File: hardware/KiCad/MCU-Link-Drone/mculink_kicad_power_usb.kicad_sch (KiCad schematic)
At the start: 39 parts, among them J9 USB4110-GF-A_REVB, U1 LPC55S69JBD64, U2 XC6227C331PR-G, Y1 16.000MHz

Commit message: updated with drone project files
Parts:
- J9: footprint mculink:GCT_USB4110-GF-A_REVB -> Connector_USB:USB_C_Receptacle_GCT_USB4110
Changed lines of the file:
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@@
 			)
 		)
-		(property "Footprint" "mculink:GCT_USB4110-GF-A_REVB"
+		(property "Footprint" "Connector_USB:USB_C_Receptacle_GCT_USB4110"
 			(at -62.23 198.12 0)
 			(effects

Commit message: worked on layout
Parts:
- J9: footprint Connector_USB:USB_C_Receptacle_GCT_USB4110 -> McuOnEclipse:USB_C_Receptacle_GCT_USB4110-GF-A
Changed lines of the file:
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@@
 			)
 		)
-		(property "Footprint" "Connector_USB:USB_C_Receptacle_GCT_USB4110"
+		(property "Footprint" "McuOnEclipse:USB_C_Receptacle_GCT_USB4110-GF-A"
 			(at -62.23 198.12 0)
 			(effects

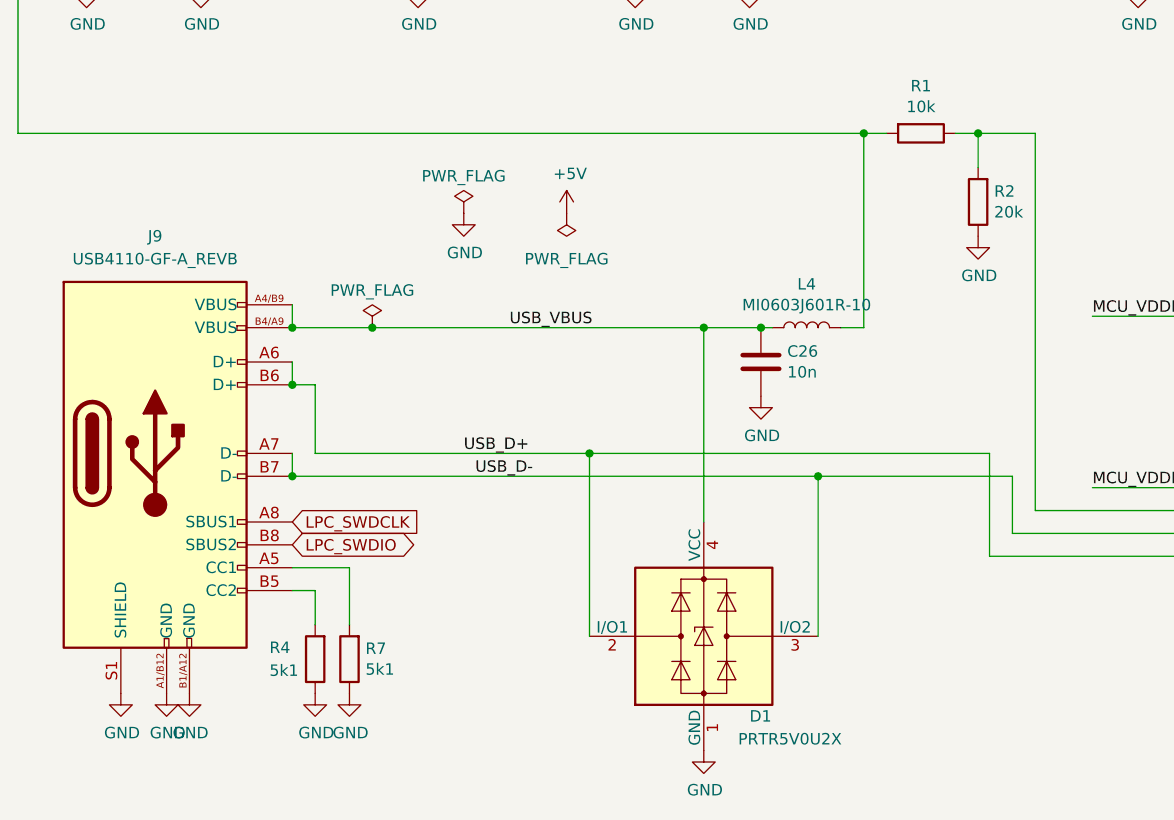
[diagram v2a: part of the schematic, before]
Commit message: fixed warnings
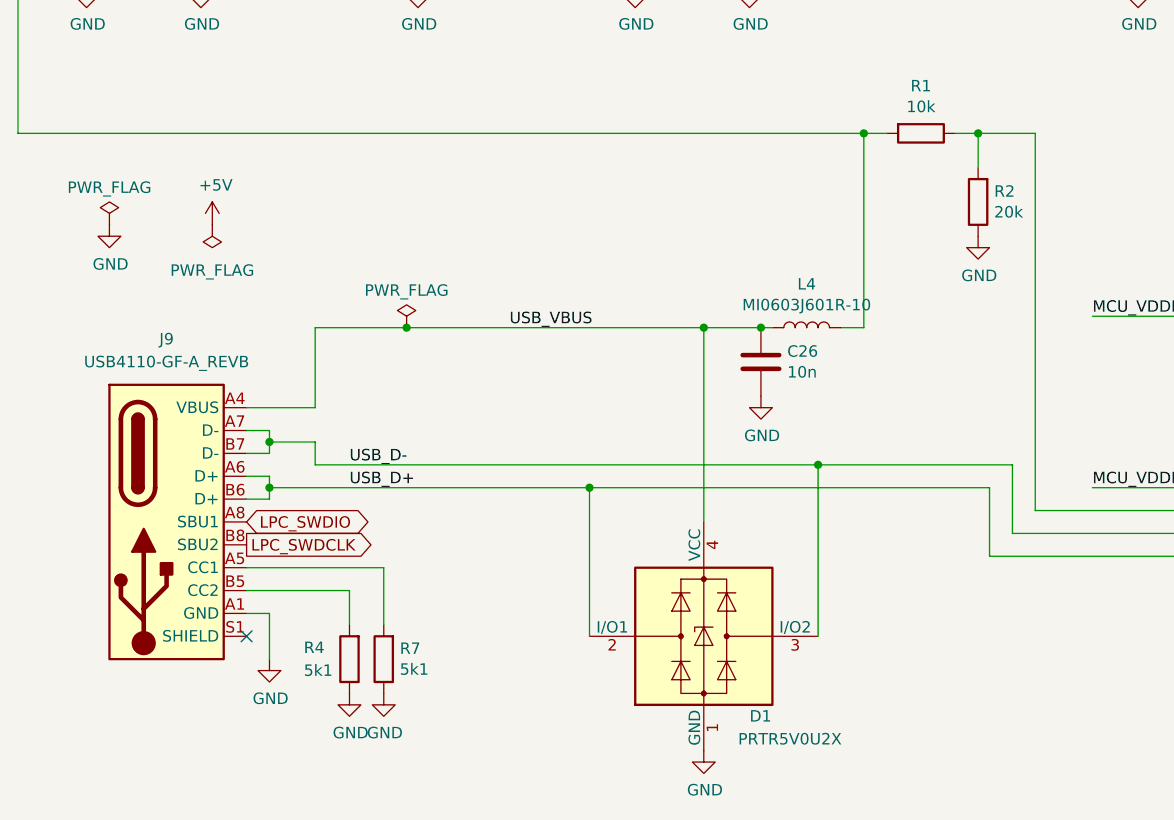
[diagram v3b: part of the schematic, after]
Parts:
- J9: symbol McuOnEclipse:USB4110-GF-A_REVB -> McuOnEclipse:USB_C_Receptacle_GCT_USB4110-GF-A; MFR (none) -> GCT; MFR# (none) -> USB4110-GF-A; mouser# (none) -> 640-USB4110-GF-A
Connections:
- net GND: now also J9.A1 (GND), J9.A12 (GND), J9.B1 (GND), J9.B12 (GND); no longer J9.A1/B12 (GND), J9.B1/A12 (GND), J9.S1 (SHIELD)
- net LPC_SWDCLK: now also J9.B8 (SBU2); no longer J9.A8 (SBUS1)
- net LPC_SWDIO: now also J9.A8 (SBU1); no longer J9.B8 (SBUS2)
- net USB_VBUS: now also J9.A4 (VBUS), J9.A9 (VBUS), J9.B4 (VBUS), J9.B9 (VBUS); no longer J9.A4/B9 (VBUS), J9.B4/A9 (VBUS)
- no-connect marks 4 -> 5
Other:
- moved on the sheet: R4, R7

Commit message: added 3D models
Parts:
- U2: footprint Package_TO_SOT_SMD:SOT-89-5 -> McuOnEclipse:SOT-89-5
- Y1: footprint mculink_kicad:CX3225GA16000D0PTVCC -> McuOnEclipse:CX3225GA16000D0PTVCC
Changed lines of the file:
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@@
 			)
 		)
-		(property "Footprint" "mculink_kicad:CX3225GA16000D0PTVCC"
+		(property "Footprint" "McuOnEclipse:CX3225GA16000D0PTVCC"
 			(at 241.3 48.26 0)
 			(effects
@@
 			)
 		)
-		(property "Footprint" "Package_TO_SOT_SMD:SOT-89-5"
+		(property "Footprint" "McuOnEclipse:SOT-89-5"
 			(at 54.61 82.55 0)
 			(effects

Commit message: fixed warnings
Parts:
- R4, R7: footprint Resistor_SMD:R_0402_1005Metric -> Resistor_SMD:R_0603_1608Metric
- U1: footprint Package_QFP:LQFP-64-1EP_10x10mm_P0.5mm_EP6.5x6.5mm_ThermalVias -> McuOnEclipse:LQFP-64-1EP_10x10mm_P0.5mm_EP5x5mm
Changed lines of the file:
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@@
 			)
 		)
-		(property "Footprint" "Package_QFP:LQFP-64-1EP_10x10mm_P0.5mm_EP6.5x6.5mm_ThermalVias"
+		(property "Footprint" "McuOnEclipse:LQFP-64-1EP_10x10mm_P0.5mm_EP5x5mm"
 			(at 186.69 24.13 0)
 			(effects
@@
 			)
 		)
-		(property "Footprint" "Package_QFP:LQFP-64-1EP_10x10mm_P0.5mm_EP6.5x6.5mm_ThermalVias"
+		(property "Footprint" "McuOnEclipse:LQFP-64-1EP_10x10mm_P0.5mm_EP5x5mm"
 			(at 146.05 100.33 0)
 			(effects
@@
 			)
 		)
-		(property "Footprint" "Resistor_SMD:R_0402_1005Metric"
+		(property "Footprint" "Resistor_SMD:R_0603_1608Metric"
 			(at 55.118 172.72 90)
 			(effects
@@
 			)
 		)
-		(property "Footprint" "Resistor_SMD:R_0402_1005Metric"
+		(property "Footprint" "Resistor_SMD:R_0603_1608Metric"
 			(at 58.928 172.72 90)
 			(effects

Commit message: improved layout
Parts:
- U1: footprint McuOnEclipse:LQFP-64-1EP_10x10mm_P0.5mm_EP5x5mm -> McuOnEclipse:LQFP-64-1EP_10x10mm_P0.5mm_EP3.5x3.5mm
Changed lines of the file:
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@@
 			)
 		)
-		(property "Footprint" "McuOnEclipse:LQFP-64-1EP_10x10mm_P0.5mm_EP5x5mm"
+		(property "Footprint" "McuOnEclipse:LQFP-64-1EP_10x10mm_P0.5mm_EP3.5x3.5mm"
 			(at 186.69 24.13 0)
 			(effects
@@
 			)
 		)
-		(property "Footprint" "McuOnEclipse:LQFP-64-1EP_10x10mm_P0.5mm_EP5x5mm"
+		(property "Footprint" "McuOnEclipse:LQFP-64-1EP_10x10mm_P0.5mm_EP3.5x3.5mm"
 			(at 146.05 100.33 0)
 			(effects

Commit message: fixed warnings
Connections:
- net GND: now also J9.S1 (SHIELD)
- no-connect marks 5 -> 4
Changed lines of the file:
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@@
+	)
+	(junction
+		(at 44.45 170.18)
+		(diameter 0)
+		(color 0 0 0 0)
 	)
 	(junction
@@
 	)
 	(no_connect
-		(at 41.91 170.18)
-	)
-	(no_connect
 		(at 152.4 137.16)
 	)
@@
 	(wire
 		(pts
-			(xy 44.45 167.64) (xy 44.45 172.72)
+			(xy 44.45 167.64) (xy 44.45 170.18)
 		)
 		(stroke
@@
 	(wire
 		(pts
+			(xy 41.91 170.18) (xy 44.45 170.18)
+		)
+		(stroke
+			(width 0)
+			(type default)
+		)
+	)
+	(wire
+		(pts
 			(xy 237.49 48.26) (xy 228.6 48.26)
 		)
@@
 		)
 		(stroke
+			(width 0)
+			(type default)
+		)
+	)
+	(wire
+		(pts
+			(xy 44.45 170.18) (xy 44.45 172.72)
+		)
+		(stroke

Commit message: updated schematics
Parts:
- C1: value 4U7 -> 4.7uF
- C18: value UL-22U -> 22u
- L2: value 4U7 -> 4u7
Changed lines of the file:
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@@
 			)
 		)
-		(property "Value" "UL-22U"
+		(property "Value" "22u"
 			(at 272.161 90.043 0)
 			(effects
@@
 			)
 		)
-		(property "Value" "4U7"
+		(property "Value" "4u7"
 			(at 228.6 82.5754 90)
 			(effects
@@
 			)
 		)
-		(property "Value" "4U7"
+		(property "Value" "4.7uF"
 			(at 53.721 43.053 0)
 			(effects
